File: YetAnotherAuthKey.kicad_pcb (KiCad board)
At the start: 2 copper layers, 31 parts, among them P1 USB_C_Plug_USB2.0, SW1 SW_Push, U1 RP2350_60QFN, U2 MCP1700x-330xxTT, Y1 ABM8-272-T3

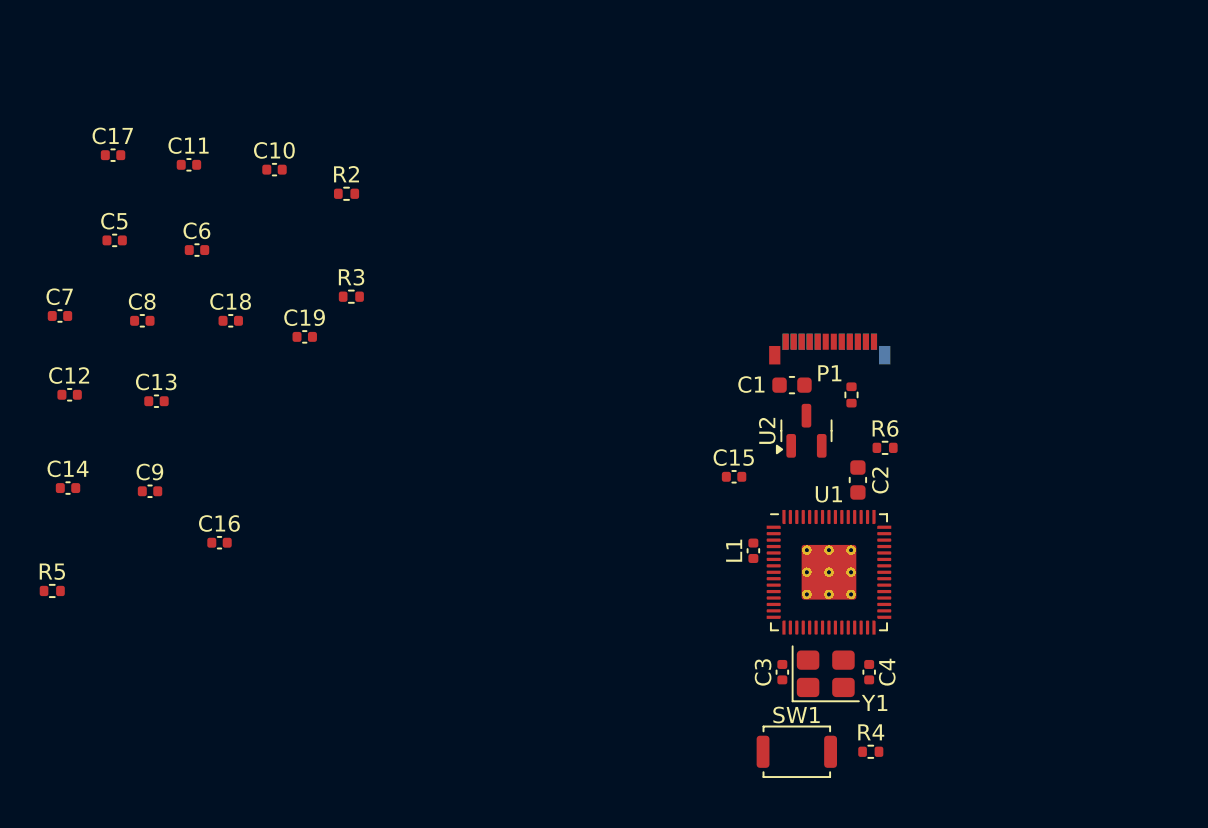
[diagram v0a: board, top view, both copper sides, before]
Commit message: place components
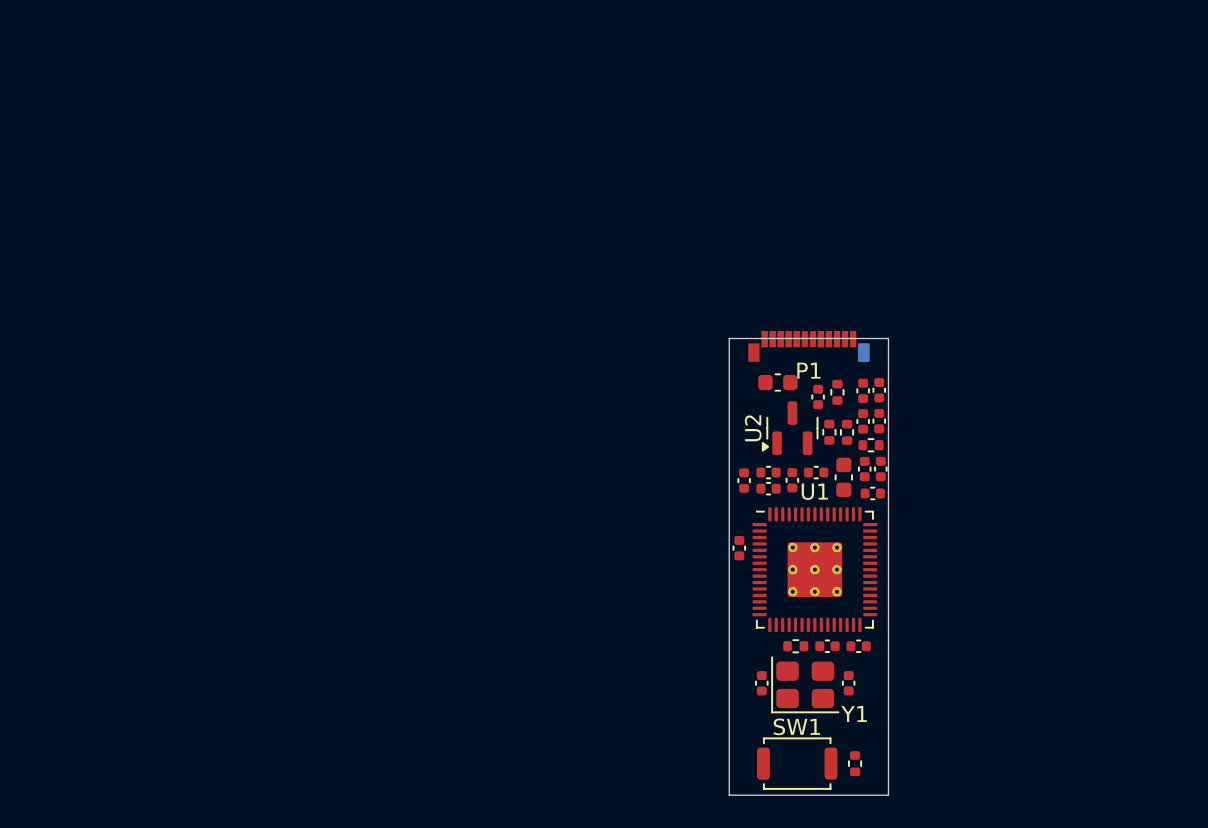
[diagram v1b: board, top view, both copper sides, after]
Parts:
- moved C17 50.4 mm to (179.3, 66.7), turned to 90 degrees
- moved C7 50.4 mm to (178.3, 66.8), turned to 90 degrees
- moved C14 50.0 mm to (178.9, 71.2)
- moved C5 48.8 mm to (178.4, 69.7), turned to 90 degrees
- moved C8 46.8 mm to (179.4, 69.7), turned to 90 degrees
- moved C12 46.5 mm to (175.5, 65.2), turned to 90 degrees
- moved R5 46.4 mm to (174.1, 80.7), turned to 180 degrees
- moved C10 45.4 mm to (176.1, 80.7)
- moved C11 45.2 mm to (179.3, 64.8), turned to 90 degrees
- moved C9 45.1 mm to (178.0, 80.7)
- moved C13 43.9 mm to (178.3, 64.9), turned to 90 degrees
- moved C16 37.4 mm to (175.4, 69.9)
- moved C6 36.9 mm to (170.9, 70.4), turned to 90 degrees
- moved C18 35.0 mm to (172.4, 70.9)
- moved R2 33.5 mm to (176.2, 67.4), turned to 90 degrees
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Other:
- board outline added: 9.9 x 28.4 mm

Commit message: finish pcb
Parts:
- removed P1: USB_C_Plug_USB2.0, Connector_USB:USB_C_Plug_Molex_105444
- removed R1: 5.1K, Resistor_SMD:R_0402_1005Metric
- added G***: LOGO, LOGO, B.Cu at (190.1, 66.8)
- added J1: USB_A, Connector_USB:USB_A_Molex_48037-2200_Horizontal, F.Cu at (190.5, 43.7)
- moved SW1 25.3 mm to (187.6, 66.5), turned to -90 degrees
- moved C6 25.1 mm to (196.1, 70.0)
- moved C12 24.8 mm to (196.2, 78.9), turned to 180 degrees
- moved C10 24.6 mm to (194.6, 64.5)
- moved C19 24.0 mm to (196.2, 73.6)
- moved C18 23.8 mm to (196.2, 72.7), turned to 180 degrees
- moved L1 23.3 mm to (193.2, 68.5), turned to -90 degrees
- moved C15 22.7 mm to (196.2, 74.6), turned to 180 degrees
- moved C11 22.6 mm to (196.2, 79.9), turned to 180 degrees
- moved C13 22.2 mm to (196.2, 78.0), turned to 180 degrees
- moved C9 21.7 mm to (194.6, 66.7)
- moved C16 21.7 mm to (196.2, 76.1), turned to 180 degrees
- moved R4 20.3 mm to (186.8, 69.8), turned to 180 degrees
- moved C14 18.2 mm to (196.2, 77.0), turned to 180 degrees
- moved C17 17.6 mm to (196.2, 71.8), turned to 180 degrees
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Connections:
- U1 pad 1: GND -> +3V3
- U1 pad 11: GND -> +3V3
- U1 pad 20: GND -> +3V3
- U1 pad 30: GND -> +3V3
- U1 pad 38: GND -> +3V3
- U1 pad 44: GND -> +3V3
- U1 pad 45: GND -> +3V3
- U1 pad 53: GND -> +3V3
- U1 pad 54: GND -> +3V3
- Y1 pad 2: unconnected-(Y1-Pad2) -> GND
- Y1 pad 4: unconnected-(Y1-Pad4) -> GND
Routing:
- net +3V3: track 0.00 -> 78.6 mm
- net +1V1: track 0.00 -> 25.2 mm
- net GND: track 0.00 -> 18.1 mm, vias 0 -> 5
- net /USB_D-: track 0.00 -> 14.3 mm, vias 0 -> 2
- net /USB_D+: track 0.00 -> 14.3 mm, vias 0 -> 2
- net Net-(C3-Pad1): track 0.00 -> 9.22 mm
- net VBUS: track 0.00 -> 5.95 mm
- net /XIN: track 0.00 -> 3.50 mm
- net Net-(U1-VREG_LX): track 0.00 -> 3.20 mm
- net Net-(U1-USB_DP): track 0.00 -> 3.11 mm
- net Net-(U1-USB_DM): track 0.00 -> 3.08 mm
- net /BOOTSEL: track 0.00 -> 2.69 mm
- net /VREG_AVDD: track 0.00 -> 2.56 mm
- net /XOUT: track 0.00 -> 1.82 mm
- net Net-(R4-Pad1): track 0.00 -> 1.32 mm
- added copper zone on B.Cu, net GND
- added copper zone on F.Cu, net GND
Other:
- board size 9.9 x 28.4 mm -> 14.4 x 34.3 mm
- board text added: "YetAnotherAuthKey v1"
